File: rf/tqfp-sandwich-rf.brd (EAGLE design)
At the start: 87.8 x 57.1 mm, 98 parts, among them IC1 PCA9555PW, IC2 MCP6002, K0 G6KU-2G-Y-TR_DC5, K1 G6KU-2G-Y-TR_DC5, K2 G6KU-2G-Y-TR_DC5, K3 G6KU-2G-Y-TR_DC5, K4 G6KU-2G-Y-TR_DC5, Q1 MMBF170, Q2 MMBF170, Q3 MMBF170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

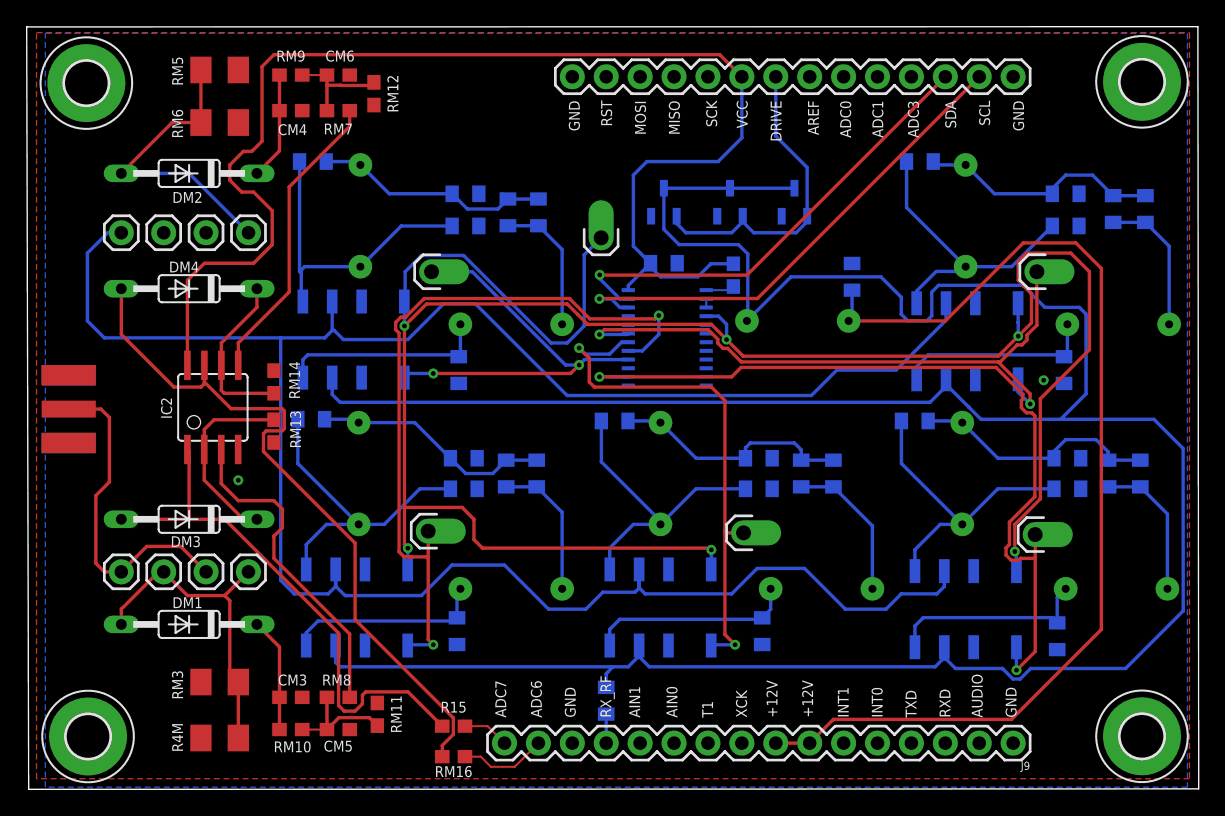
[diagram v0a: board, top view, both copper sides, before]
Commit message: Add capacitor on the MCP6002 power rail
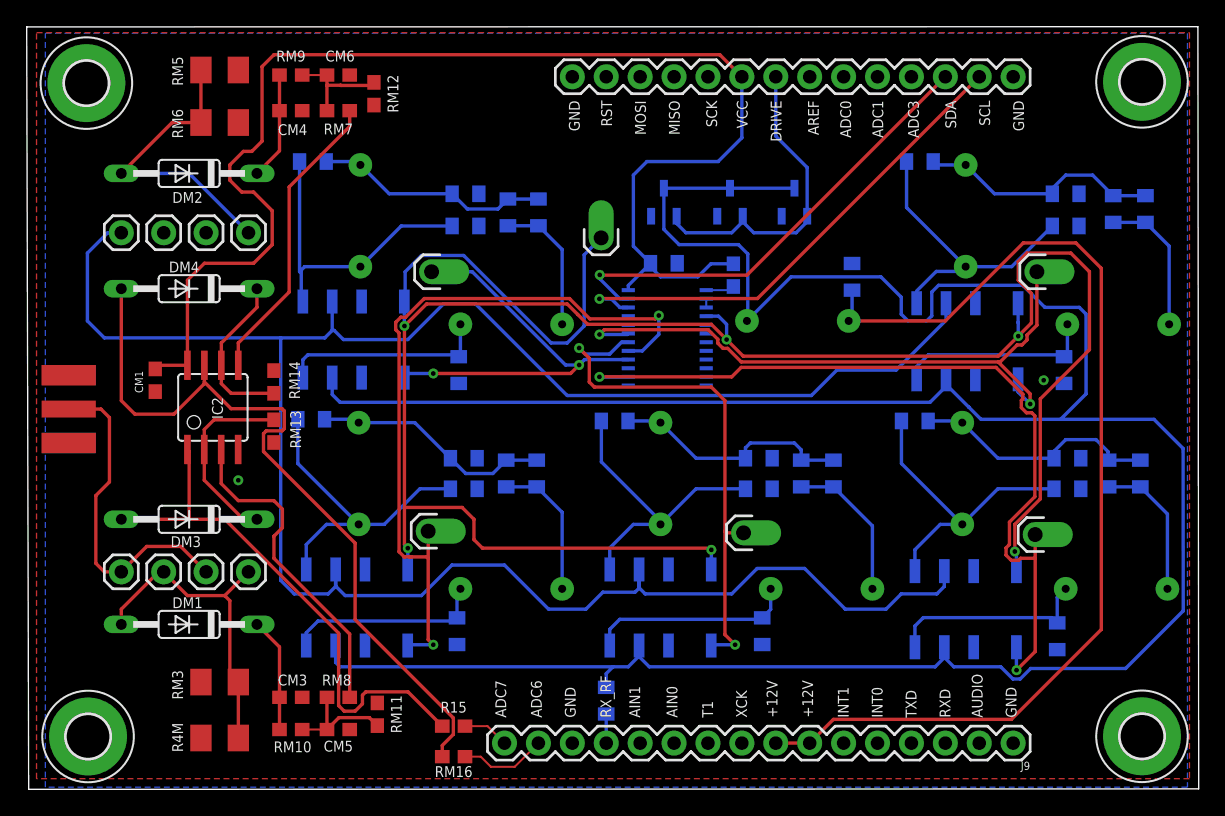
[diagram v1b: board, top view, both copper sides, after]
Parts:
- added CM1: 0.1uF, SparkFun-Capacitors:0603
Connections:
- net GND: now also CM1.2
- net VCC: now also CM1.1
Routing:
- net N$6: track 53.1 -> 57.7 mm
- net VCC: track 98.2 -> 100.8 mm
- net RX_RF: track 221.2 -> 219.1 mm
- net N$2: track 18.2 -> 17.7 mm
